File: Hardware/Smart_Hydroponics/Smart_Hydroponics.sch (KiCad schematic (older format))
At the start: 36 parts, among them J2 BNC, J3 Water Level MAX, J4 Water Level MIN, J5 Solution Temperature, U1 ESP32-WROOM, U2 AP1509, U3 MC33078, U4 MCP3421, U5 MCP1501, U6 SHT31

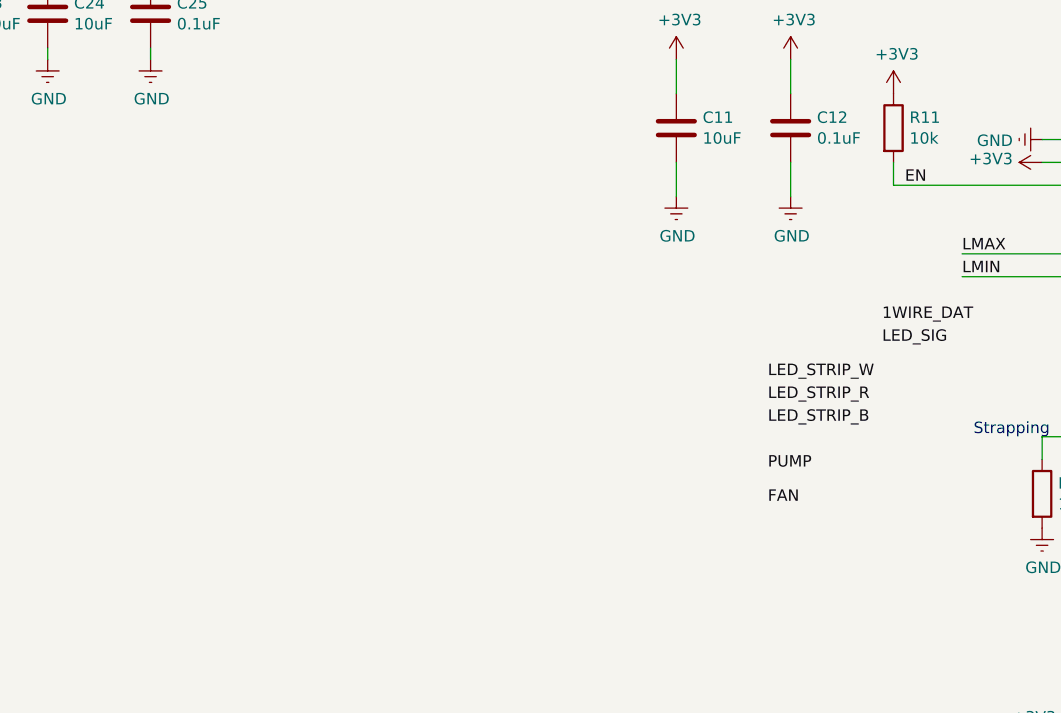
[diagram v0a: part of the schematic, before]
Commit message: Changes in schematics I didn't push before by accident.
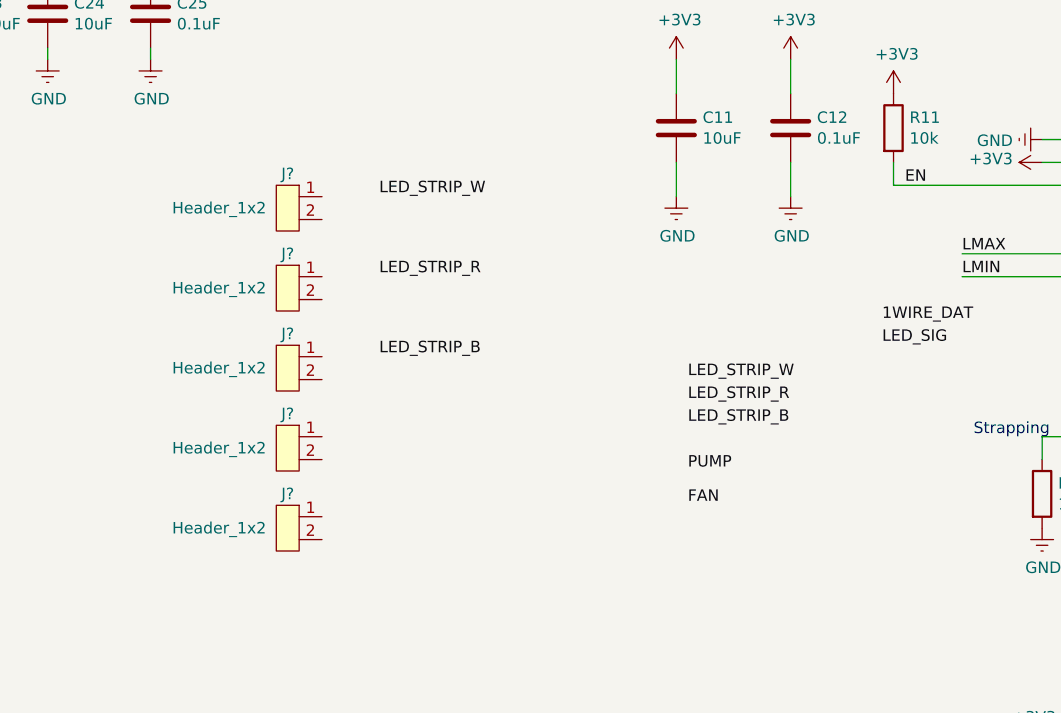
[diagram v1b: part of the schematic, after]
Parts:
- added J? (x5): Header_1x2, MRS_Connectors:Header_1x02_P2.54mm, symbol MRS_Connectors:Header_1x2
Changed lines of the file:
@@
 Text Label 7150 3100 0    50   ~ 0
 LED_SIG
-Text Label 6650 3250 0    50   ~ 0
+Text Label 6300 3250 0    50   ~ 0
 LED_STRIP_W
-Text Label 6650 3350 0    50   ~ 0
+Text Label 6300 3350 0    50   ~ 0
 LED_STRIP_R
-Text Label 6650 3450 0    50   ~ 0
+Text Label 6300 3450 0    50   ~ 0
 LED_STRIP_B
-Text Label 6650 3650 0    50   ~ 0
+Text Label 6300 3650 0    50   ~ 0
 PUMP
-Text Label 6650 3800 0    50   ~ 0
+Text Label 6300 3800 0    50   ~ 0
 FAN
 $Comp
@@
 	1    0    0    -1
 $EndComp
+$Comp
+L MRS_Connectors:Header_1x2 J?
+U 1 1 5D2998AD
+P 4550 2500
+F 0 "J?" H 4550 2650 50  0000 C CNN
+F 1 "Header_1x2" H 4850 2500 50  0000 C CNN
+F 2 "MRS_Connectors:Header_1x02_P2.54mm" H 4550 2250 50  0001 C CNN
+F 3 "" H 4100 2200 50  0001 C CNN
+	1    4550 2500
+	-1   0    0    -1
+$EndComp
+$Comp
+L MRS_Connectors:Header_1x2 J?
+U 1 1 5D299AFA
+P 4550 2850
+F 0 "J?" H 4550 3000 50  0000 C CNN
+F 1 "Header_1x2" H 4850 2850 50  0000 C CNN
+F 2 "MRS_Connectors:Header_1x02_P2.54mm" H 4550 2600 50  0001 C CNN
+F 3 "" H 4100 2550 50  0001 C CNN
+	1    4550 2850
+	-1   0    0    -1
+$EndComp
+$Comp
+L MRS_Connectors:Header_1x2 J?
+U 1 1 5D299B62
+P 4550 3200
+F 0 "J?" H 4550 3350 50  0000 C CNN
+F 1 "Header_1x2" H 4850 3200 50  0000 C CNN
+F 2 "MRS_Connectors:Header_1x02_P2.54mm" H 4550 2950 50  0001 C CNN
+F 3 "" H 4100 2900 50  0001 C CNN
+	1    4550 3200
+	-1   0    0    -1
+$EndComp
+$Comp
+L MRS_Connectors:Header_1x2 J?
+U 1 1 5D299BD0
+P 4550 3550
+F 0 "J?" H 4550 3700 50  0000 C CNN
+F 1 "Header_1x2" H 4850 3550 50  0000 C CNN
+F 2 "MRS_Connectors:Header_1x02_P2.54mm" H 4550 3300 50  0001 C CNN
+F 3 "" H 4100 3250 50  0001 C CNN
+	1    4550 3550
+	-1   0    0    -1
+$EndComp
+$Comp
+L MRS_Connectors:Header_1x2 J?
+U 1 1 5D299C40
+P 4550 3900
+F 0 "J?" H 4550 4050 50  0000 C CNN
+F 1 "Header_1x2" H 4850 3900 50  0000 C CNN
+F 2 "MRS_Connectors:Header_1x02_P2.54mm" H 4550 3650 50  0001 C CNN
+F 3 "" H 4100 3600 50  0001 C CNN
+	1    4550 3900
+	-1   0    0    -1
+$EndComp
+Text Label 4950 2450 0    50   ~ 0
+LED_STRIP_W
+Text Label 4950 2800 0    50   ~ 0
+LED_STRIP_R
+Text Label 4950 3150 0    50   ~ 0
+LED_STRIP_B
 $EndSCHEMATC
